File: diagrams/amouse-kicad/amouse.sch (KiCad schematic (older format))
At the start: 10 parts, among them J1 USB_A, J2 DB9_Male_MountingHoles, U1 Pico, U2 MAX3232

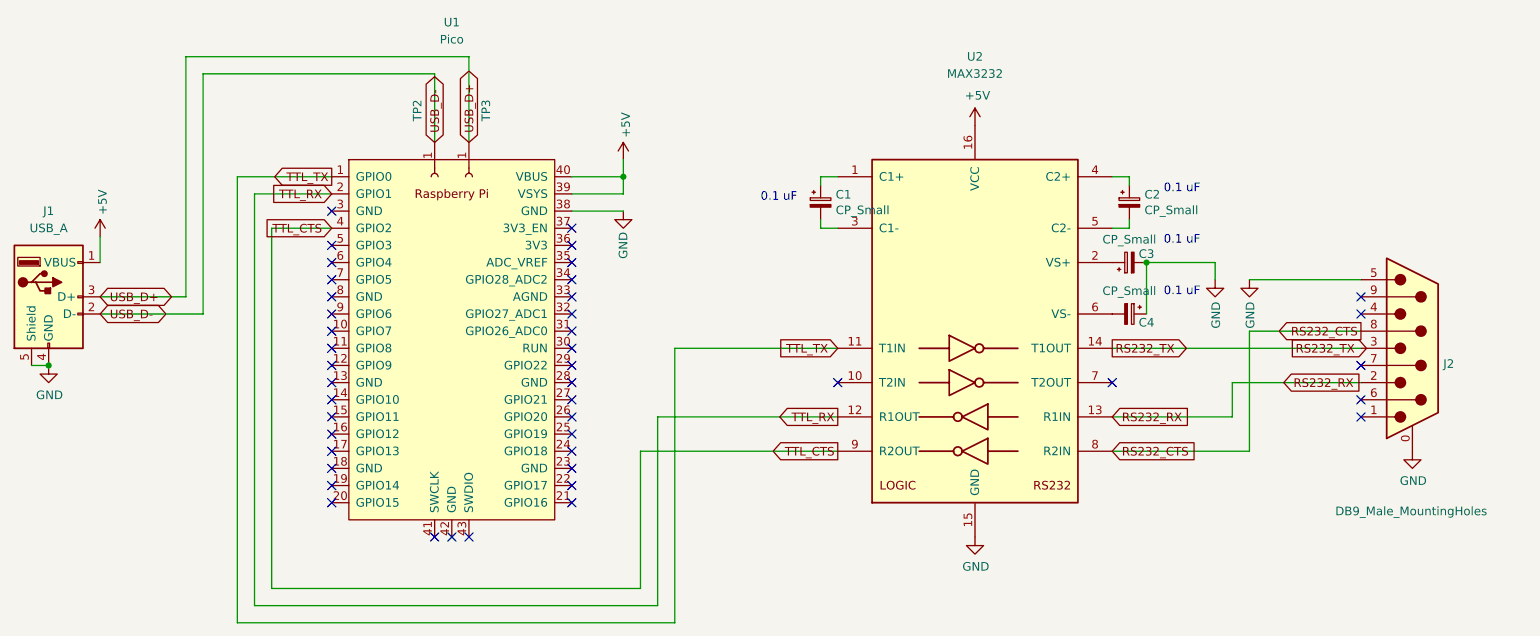
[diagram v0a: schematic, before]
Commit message: Added cbypass capacitor to Pico schematic, minor changes.
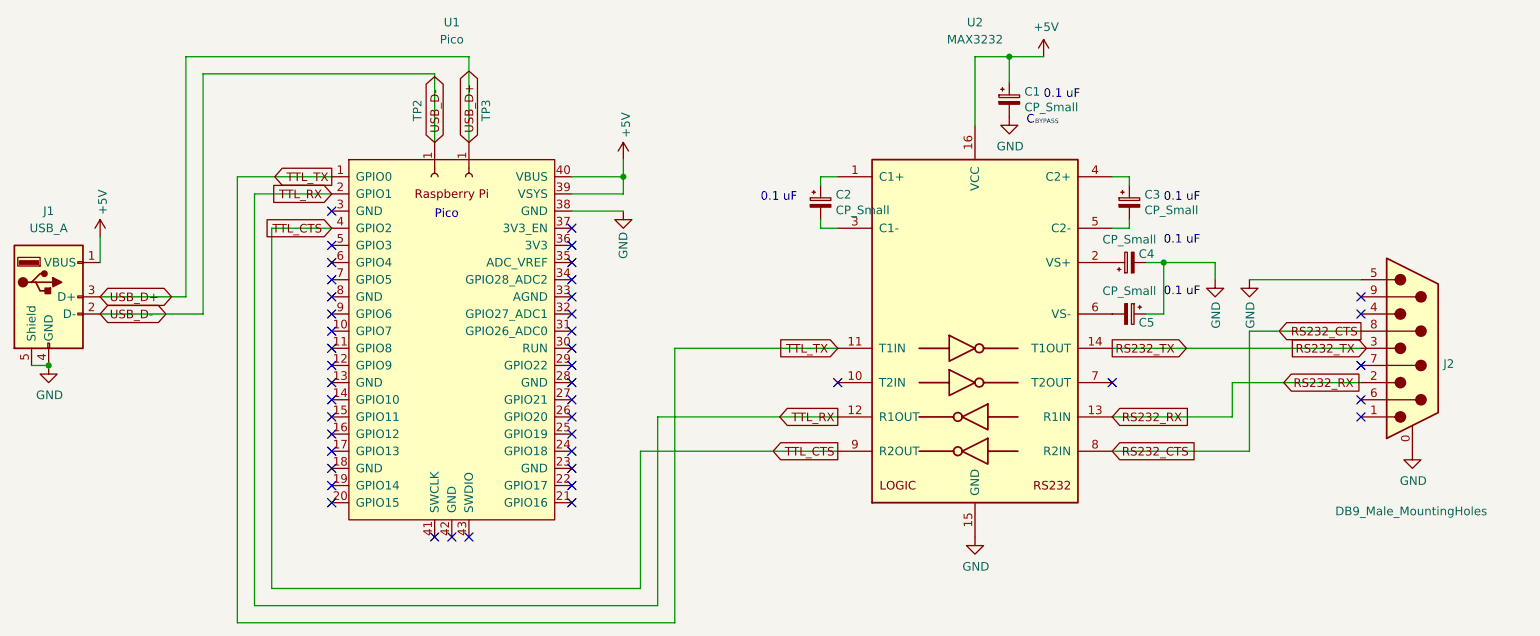
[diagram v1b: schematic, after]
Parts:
- added C1: CP_Small, symbol Device:CP_Small
- renumbered C1 to C2, C2 to C3, C3 to C4, C4 to C5
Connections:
- net +5V: now also C1.1
- net GND: now also C1.2
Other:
- note added: "BYPASS\n"
- note added: "C"
- note added: "Pico"
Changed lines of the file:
@@
 Title "Anachro Mouse, USB to Serial Mouse Adapter"
 Date "2021-07-27"
-Rev "1"
+Rev "2"
 Comp "github.com/Aviancer/amouse"
 Comment1 "twitter.com/skyvian"
@@
 	1750 4000 1850 4000
 Connection ~ 1850 4000
-Text GLabel 2150 3600 2    50   BiDi ~ 0
-USB_D+
-Text GLabel 2150 3700 2    50   BiDi ~ 0
-USB_D-
 $Comp
 L power:GND #PWR?
@@
 U 1 1 60DC4834
 P 7250 3800
-F 0 "U2" H 7250 5400 50  0000 C CNN
-F 1 "MAX3232" H 7250 5300 50  0000 C CNN
+F 0 "U2" H 7250 5600 50  0000 C CNN
+F 1 "MAX3232" H 7250 5500 50  0000 C CNN
 F 2 "" H 7300 2750 50  0001 L CNN
 F 3 "https://datasheets.maximintegrated.com/en/ds/MAX3222-MAX3241.pdf" H 7250 3900 50  0001 C CNN
@@
 Text Notes 8350 3300 0    50   ~ 0
 0.1 uF
-Text Notes 8350 3000 0    50   ~ 0
+Text Notes 8350 3050 0    50   ~ 0
 0.1 uF
 Text Notes 6000 3050 0    50   ~ 0
@@
 	8050 2900 8150 2900
 $Comp
-L Device:CP_Small C1
+L Device:CP_Small C2
 U 1 1 60DCDCB9
 P 6350 3050
-F 0 "C1" H 6438 3096 50  0000 L CNN
+F 0 "C2" H 6438 3096 50  0000 L CNN
 F 1 "CP_Small" H 6438 3005 50  0000 L CNN
 F 2 "" H 6350 3050 50  0001 C CNN
@@
 $EndComp
 $Comp
-L Device:CP_Small C2
+L Device:CP_Small C3
 U 1 1 60DD17D0
 P 8150 3050
-F 0 "C2" H 8238 3096 50  0000 L CNN
+F 0 "C3" H 8238 3096 50  0000 L CNN
 F 1 "CP_Small" H 8238 3005 50  0000 L CNN
 F 2 "" H 8150 3050 50  0001 C CNN
@@
 RS232_TX
 $Comp
-L Device:CP_Small C4
+L Device:CP_Small C5
 U 1 1 60DD1E84
 P 8150 3700
-F 0 "C4" V 8200 3800 50  0000 C CNN
+F 0 "C5" V 8200 3800 50  0000 C CNN
 F 1 "CP_Small" V 8016 3700 50  0000 C CNN
 F 2 "" H 8150 3700 50  0001 C CNN
@@
 $EndComp
 $Comp
-L Device:CP_Small C3
+L Device:CP_Small C4
 U 1 1 60DCF2E8
 P 8150 3400
-F 0 "C3" V 8200 3300 50  0000 C CNN
+F 0 "C4" V 8200 3300 50  0000 C CNN
 F 1 "CP_Small" V 8284 3400 50  0000 C CNN
 F 2 "" H 8150 3400 50  0001 C CNN
@@
 L power:+5V #PWR?
 U 1 1 60DCBE28
-P 7250 2600
-F 0 "#PWR?" H 7250 2450 50  0001 C CNN
-F 1 "+5V" H 7265 2773 50  0000 C CNN
-F 2 "" H 7250 2600 50  0001 C CNN
-F 3 "" H 7250 2600 50  0001 C CNN
-	1    7250 2600
+P 7650 2200
+F 0 "#PWR?" H 7650 2050 50  0001 C CNN
+F 1 "+5V" H 7665 2373 50  0000 C CNN
+F 2 "" H 7650 2200 50  0001 C CNN
+F 3 "" H 7650 2200 50  0001 C CNN
+	1    7650 2200
 	1    0    0    -1
 $EndComp
@@
 	4900 3100 5200 3100
 Wire Wire Line
-	8250 3700 8250 3400
-Wire Wire Line
-	8250 3400 8650 3400
-Connection ~ 8250 3400
+	8350 3700 8350 3400
+Wire Wire Line
+	8250 3400 8350 3400
 Wire Wire Line
 	8650 3400 8650 3500
@@
 Wire Wire Line
 	8850 3500 9500 3500
+Connection ~ 8350 3400
+Wire Wire Line
+	8350 3400 8650 3400
+Wire Wire Line
+	8250 3700 8350 3700
+$Comp
+L power:GND #PWR?
+U 1 1 6103CC7F
+P 7450 2550
+F 0 "#PWR?" H 7450 2300 50  0001 C CNN
+F 1 "GND" H 7455 2377 50  0000 C CNN
+F 2 "" H 7450 2550 50  0001 C CNN
+F 3 "" H 7450 2550 50  0001 C CNN
+	1    7450 2550
+	1    0    0    -1
+$EndComp
+Wire Wire Line
+	7250 2600 7250 2200
+Wire Wire Line
+	7250 2200 7450 2200
+$Comp
+L Device:CP_Small C1
+U 1 1 6103B4CE
+P 7450 2450
+F 0 "C1" H 7538 2496 50  0000 L CNN
+F 1 "CP_Small" H 7538 2405 50  0000 L CNN
+F 2 "" H 7450 2450 50  0001 C CNN
+F 3 "~" H 7450 2450 50  0001 C CNN
+	1    7450 2450
+	1    0    0    -1
+$EndComp
+Wire Wire Line
+	7450 2350 7450 2200
+Connection ~ 7450 2200
+Wire Wire Line
+	7450 2200 7650 2200
+Text Notes 7650 2450 0    50   ~ 0
+0.1 uF
+Text GLabel 2150 3700 2    50   BiDi ~ 0
+USB_D-
+Text GLabel 2150 3600 2    50   BiDi ~ 0
+USB_D+
+Text Notes 4100 3150 0    50   ~ 0
+Pico
+Text Notes 7550 2600 0    50   ~ 0
+C
+Text Notes 7600 2600 0    26   ~ 0
+BYPASS\n
 $EndSCHEMATC
